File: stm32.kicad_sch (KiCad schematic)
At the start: 4 parts, among them U103 STM32G071KBTx

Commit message: githubstart
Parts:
- removed C801: 1n, Capacitor_SMD:C_0603_1608Metric_Pad1.08x0.95mm_HandSolder, symbol Device:C
- removed C801: 100n, Capacitor_SMD:C_0603_1608Metric_Pad1.08x0.95mm_HandSolder, symbol Device:C
- added C801: 1n, Capacitor_SMD:C_0603_1608Metric_Pad1.08x0.95mm_HandSolder, symbol Device:C
- added C801: 100n, Capacitor_SMD:C_0603_1608Metric_Pad1.08x0.95mm_HandSolder, symbol Device:C
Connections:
- net 3V3: now also C801.1, C801.1
- net GND: now also C801.2, C801.2

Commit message: asdf
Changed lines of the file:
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@@
     (stroke (width 0) (type default))
+  )
+  (hierarchical_label "REN" (shape input) (at 158.75 116.84 0) (fields_autoplaced)
+    (effects (font (size 1.27 1.27)) (justify left))
   )
   (hierarchical_label "ADC_IN7" (shape input) (at 149.86 87.63 0) (fields_autoplaced)
@@
     (effects (font (size 1.27 1.27)) (justify left))
   )
+  (hierarchical_label "DEN" (shape input) (at 160.02 111.76 0) (fields_autoplaced)
+    (effects (font (size 1.27 1.27)) (justify left))
+  )

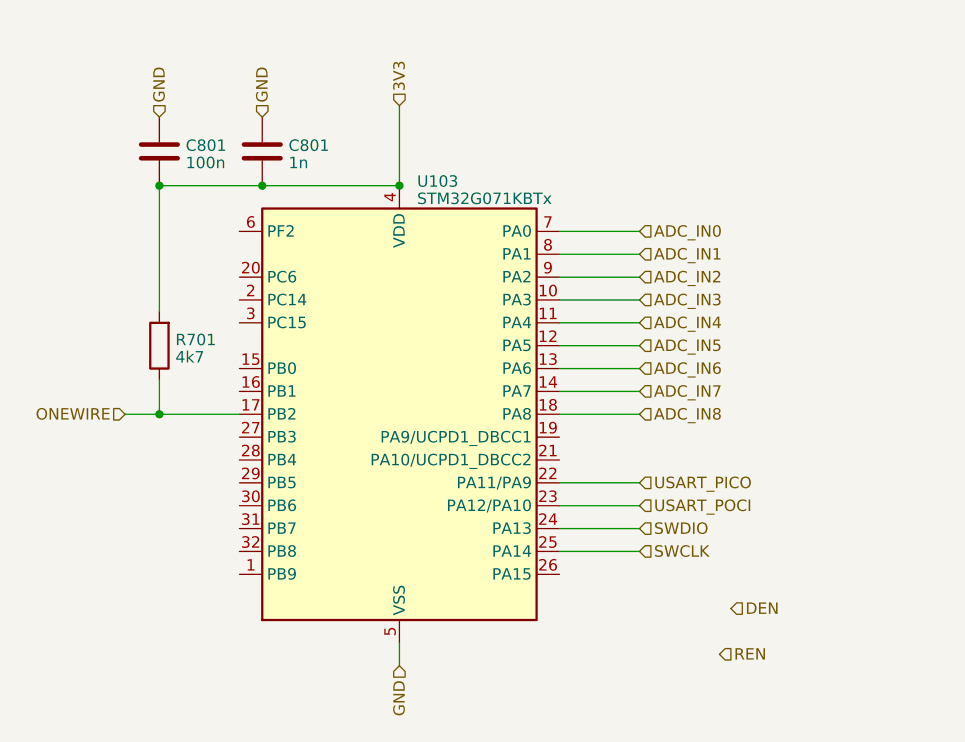
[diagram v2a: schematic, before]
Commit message: aisler DRC und preise
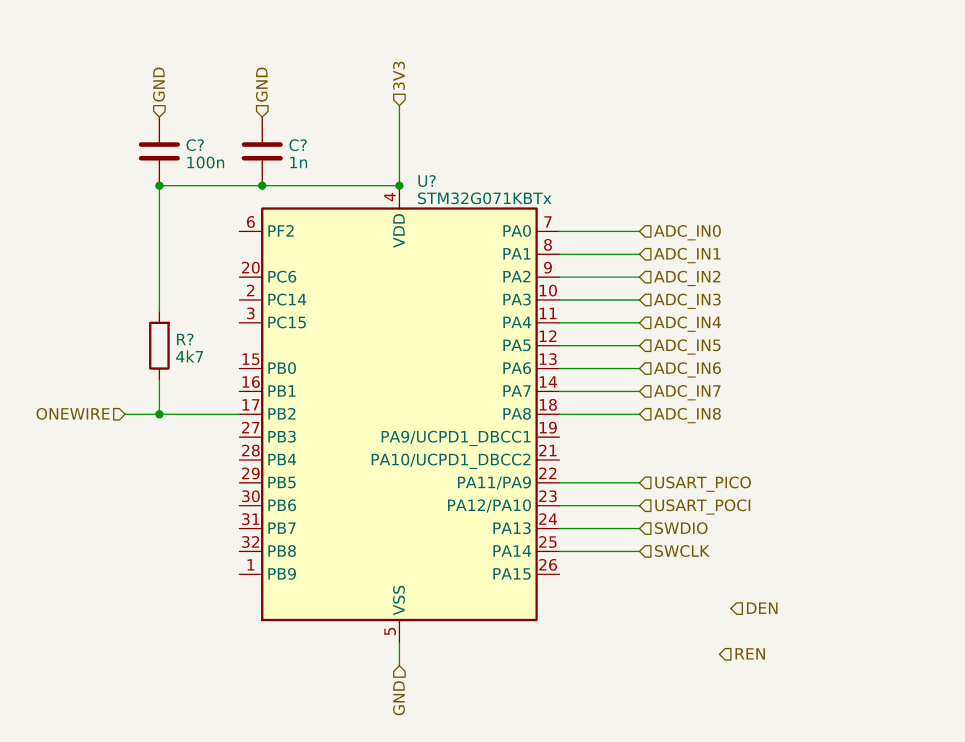
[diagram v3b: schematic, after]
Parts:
- renumbered C801 to C?, R701 to R?, U103 to U?
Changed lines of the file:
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@@
   (symbol (lib_id "MCU_ST_STM32G0:STM32G071KBTx") (at 123.19 90.17 0) (unit 1)
     (in_bom yes) (on_board yes) (dnp no) (fields_autoplaced)
-    (property "Reference" "U103" (at 125.1459 64.3001 0)
+    (property "Reference" "U?" (at 125.1459 64.3001 0)
       (effects (font (size 1.27 1.27)) (justify left))
     )
@@
       (project "stm32"
         (path "/a2a88a52-8cdb-4122-8d15-41075823ed07"
-          (reference "U103") (unit 1)
+          (reference "U?") (unit 1)
         )
       )
       (project "main"
         (path "/a7d525ca-c4cb-4a7a-8337-8afd7514bbeb"
-          (reference "U103") (unit 1)
+          (reference "U?") (unit 1)
         )
         (path "/a7d525ca-c4cb-4a7a-8337-8afd7514bbeb/608fadb2-7436-4bb6-b36c-1e70f65483d8"
-          (reference "U103") (unit 1)
+          (reference "U?") (unit 1)
         )
       )
       (project "hw_voltmod"
         (path "/aba5ff33-6d0a-4fec-b36e-20121d176c3c/598d7000-f460-468d-8276-28163f3735c3"
-          (reference "U8") (unit 1)
+          (reference "U2") (unit 1)
         )
       )
@@
   (symbol (lib_id "Device:R") (at 96.52 82.55 180) (unit 1)
     (in_bom yes) (on_board yes) (dnp no) (fields_autoplaced)
-    (property "Reference" "R701" (at 98.298 81.9063 0)
+    (property "Reference" "R?" (at 98.298 81.9063 0)
       (effects (font (size 1.27 1.27)) (justify right))
     )
@@
       (project "stm32"
         (path "/a2a88a52-8cdb-4122-8d15-41075823ed07"
-          (reference "R701") (unit 1)
+          (reference "R?") (unit 1)
         )
       )
       (project "main"
         (path "/a7d525ca-c4cb-4a7a-8337-8afd7514bbeb"
-          (reference "R701") (unit 1)
+          (reference "R?") (unit 1)
         )
         (path "/a7d525ca-c4cb-4a7a-8337-8afd7514bbeb/a66b9f2e-6ae3-4ea2-ba88-5754b149371d"
-          (reference "R109") (unit 1)
+          (reference "R?") (unit 1)
         )
         (path "/a7d525ca-c4cb-4a7a-8337-8afd7514bbeb/608fadb2-7436-4bb6-b36c-1e70f65483d8"
-          (reference "R137") (unit 1)
+          (reference "R?") (unit 1)
         )
       )
       (project "hw_voltmod"
         (path "/aba5ff33-6d0a-4fec-b36e-20121d176c3c/598d7000-f460-468d-8276-28163f3735c3"
-          (reference "R54") (unit 1)
+          (reference "R3") (unit 1)
         )
       )
@@
   (symbol (lib_id "Device:C") (at 107.95 60.96 180) (unit 1)
     (in_bom yes) (on_board yes) (dnp no) (fields_autoplaced)
-    (property "Reference" "C801" (at 110.871 60.3163 0)
+    (property "Reference" "C?" (at 110.871 60.3163 0)
       (effects (font (size 1.27 1.27)) (justify right))
     )
@@
       (project "stm32"
         (path "/a2a88a52-8cdb-4122-8d15-41075823ed07"
-          (reference "C801") (unit 1)
+          (reference "C?") (unit 1)
         )
       )
       (project "main"
         (path "/a7d525ca-c4cb-4a7a-8337-8afd7514bbeb"
-          (reference "C801") (unit 1)
+          (reference "C?") (unit 1)
         )
         (path "/a7d525ca-c4cb-4a7a-8337-8afd7514bbeb/a66b9f2e-6ae3-4ea2-ba88-5754b149371d"
-          (reference "C103") (unit 1)
+          (reference "C?") (unit 1)
         )
         (path "/a7d525ca-c4cb-4a7a-8337-8afd7514bbeb/608fadb2-7436-4bb6-b36c-1e70f65483d8"
-          (reference "C121") (unit 1)
+          (reference "C?") (unit 1)
         )
       )
       (project "hw_voltmod"
         (path "/aba5ff33-6d0a-4fec-b36e-20121d176c3c/598d7000-f460-468d-8276-28163f3735c3"
-          (reference "C21") (unit 1)
+          (reference "C5") (unit 1)
         )
       )
@@
   (symbol (lib_id "Device:C") (at 96.52 60.96 180) (unit 1)
     (in_bom yes) (on_board yes) (dnp no) (fields_autoplaced)
-    (property "Reference" "C801" (at 99.441 60.3163 0)
+    (property "Reference" "C?" (at 99.441 60.3163 0)
       (effects (font (size 1.27 1.27)) (justify right))
     )
@@
       (project "stm32"
         (path "/a2a88a52-8cdb-4122-8d15-41075823ed07"
-          (reference "C801") (unit 1)
+          (reference "C?") (unit 1)
         )
       )
       (project "main"
         (path "/a7d525ca-c4cb-4a7a-8337-8afd7514bbeb"
-          (reference "C801") (unit 1)
+          (reference "C?") (unit 1)
         )
         (path "/a7d525ca-c4cb-4a7a-8337-8afd7514bbeb/a66b9f2e-6ae3-4ea2-ba88-5754b149371d"
-          (reference "C103") (unit 1)
+          (reference "C?") (unit 1)
         )
         (path "/a7d525ca-c4cb-4a7a-8337-8afd7514bbeb/608fadb2-7436-4bb6-b36c-1e70f65483d8"
-          (reference "C120") (unit 1)
+          (reference "C?") (unit 1)
         )
       )
       (project "hw_voltmod"
         (path "/aba5ff33-6d0a-4fec-b36e-20121d176c3c/598d7000-f460-468d-8276-28163f3735c3"
-          (reference "C20") (unit 1)
+          (reference "C4") (unit 1)
         )
       )
